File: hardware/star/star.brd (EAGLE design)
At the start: 139.4 x 187.9 mm, 170 parts, among them IC1 MAX481CSA, IC2 LD117AS12TR, IC22 LD117AS12TR, IC3 74HCT08D, IC4 7404D, IC8 MAX481CSA, K1 T90-12VDC-TL-A, K2 T90-12VDC-TL-A, K3 T90-12VDC-TL-A, K5 AQG22110, K6 AQG22110, Q1 35A/25V/8.5mΩ, Q2 35A/25V/8.5mΩ, Q3 35A/25V/8.5mΩ, Q4 35A/25V/8.5mΩ, T1 T_PNP_MMBT5401_CHANGJ_SOT23-B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, T2 T_PNP_MMBT5401_CHANGJ_SOT23-B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, T3 T_PNP_MMBT5401_CHANGJ_SOT23-B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, T4 T_PNP_MMBT5401_CHANGJ_SOT23-B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, U1 TCLT1600

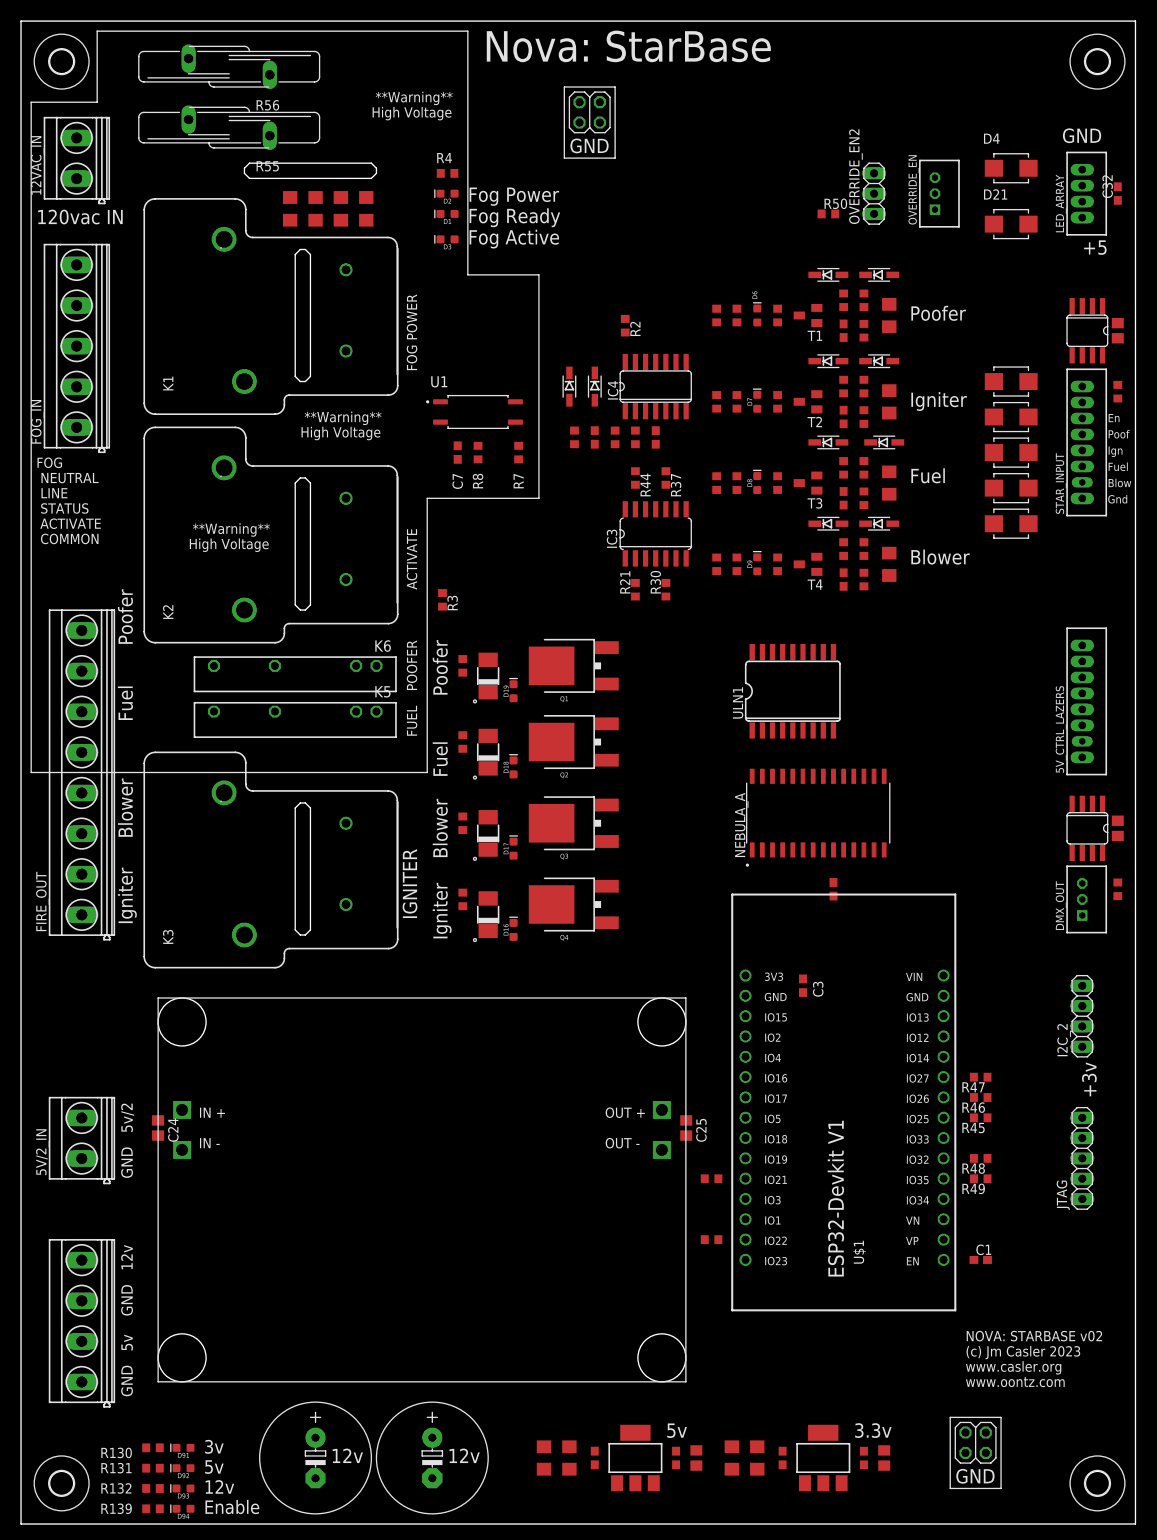
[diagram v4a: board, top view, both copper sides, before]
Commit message: Manual Routing Complete for v2
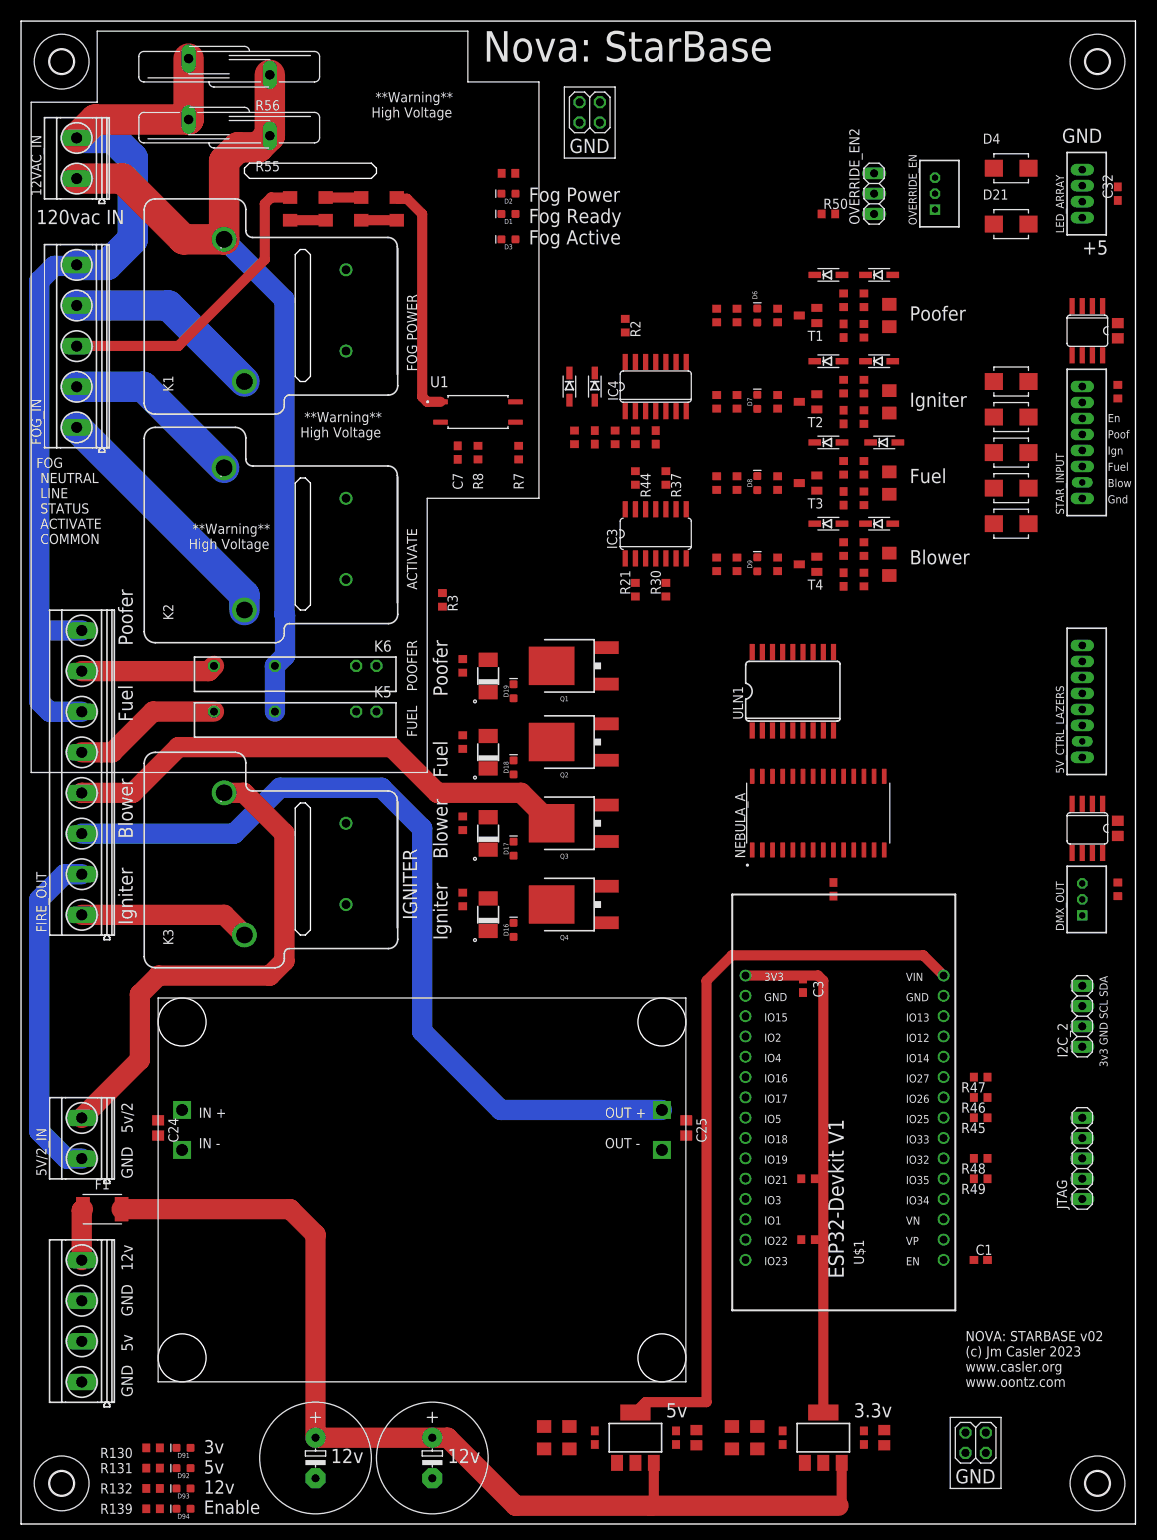
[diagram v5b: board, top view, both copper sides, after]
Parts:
- added F1: MF-MSMF-STYLE2_1, Fuse:FUSC4632X160
- moved R26 12.1 mm to (98.4, 35.6), turned to 0 degrees
- moved R27 12.1 mm to (98.4, 43.2), turned to 0 degrees
- moved D1 7.62 mm to (61.0, 163.8)
- moved D2 7.62 mm to (61.0, 166.4)
- moved D3 7.62 mm to (61.0, 160.7)
- moved R4 7.62 mm to (61.0, 168.9)
- moved R10 3.81 mm to (47.0, 164.5)
- moved C10 2.54 mm to (65.4, 10.8)
- moved C11 2.54 mm to (92.1, 10.8)
- moved C12 2.54 mm to (88.9, 10.8)
- moved C2 2.54 mm to (81.9, 10.8)
- moved C35 2.54 mm to (105.4, 10.8)
- moved C36 2.54 mm to (95.2, 10.8)
- moved C4 2.54 mm to (84.5, 10.8)
- moved C5 2.54 mm to (71.8, 10.8)
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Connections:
- new net N$59: F1.1, POWER_IN.4
- net +12V: now also C35.1, C6.1, F1.2, IC22.3; no longer POWER_IN.4
- net +5V: no longer C35.1, C6.1, IC22.3
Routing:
- net +12V: track 0.00 -> 130.9 mm
- net 120_NEUTRAL: track 0.00 -> 118.4 mm
- net 120_LINE: track 0.00 -> 108.8 mm
- net +14V: track 0.00 -> 106.5 mm
- net +5V: track 0.00 -> 94.2 mm
- net N$51: track 0.00 -> 65.1 mm
- net +3V3: track 0.00 -> 64.0 mm
- net +5V/2: track 0.00 -> 63.9 mm
- net GND3: track 0.00 -> 42.3 mm
- net N$7: track 0.00 -> 38.5 mm
- net N$15: track 0.00 -> 31.5 mm
- net N$11: track 0.00 -> 29.5 mm
- net N$14: track 0.00 -> 24.9 mm
- net N$13: track 0.00 -> 22.6 mm
- net N$53: track 0.00 -> 21.4 mm
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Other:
- board text added: "3v3 GND SCL SDA"
- board text removed: "+3v"

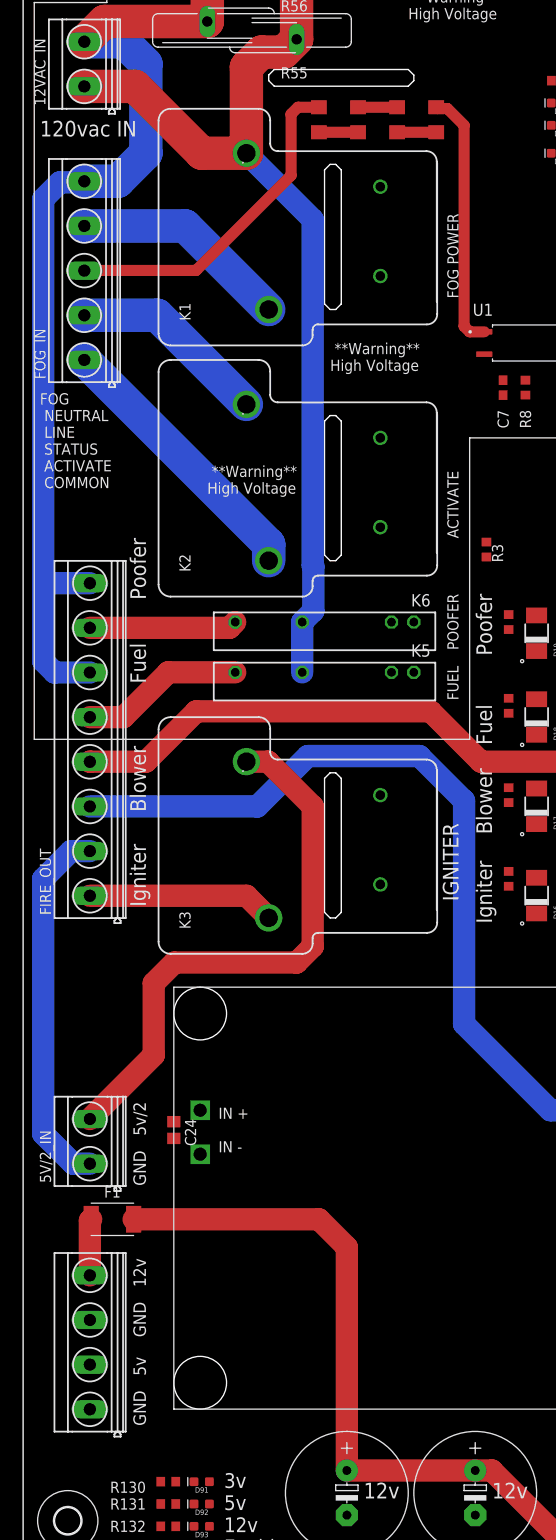
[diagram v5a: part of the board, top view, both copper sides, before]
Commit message: Swapped 1.5A fuse with 5A fuse
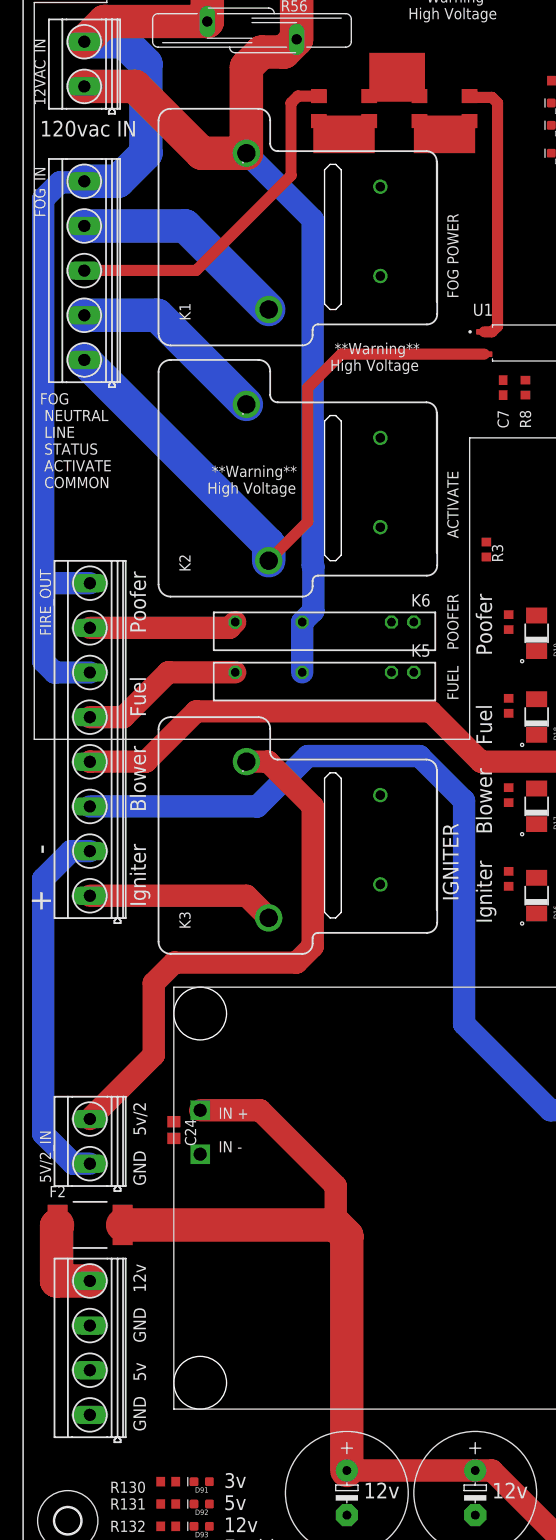
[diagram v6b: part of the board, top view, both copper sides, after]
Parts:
- removed F1: MF-MSMF-STYLE2_1, Fuse:FUSC4632X160
- added F2: 2920L200, 2920L200:SMD050F
- moved R10 4.02 mm to (50.8, 165.7)
- moved R11 2.84 mm to (45.1, 165.7)
- moved R12 1.80 mm to (39.4, 165.7)
- moved R13 1.27 mm to (33.7, 165.7)
- moved POWER_IN 0.63 mm to (7.62, 24.8)
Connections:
- net +12V: now also F2.2; no longer F1.2
- net N$59: now also F2.1; no longer F1.1
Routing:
- net N$15: track 31.5 -> 74.7 mm
- net +12V: track 130.9 -> 156.1 mm
- net N$59: track 6.43 -> 10.2 mm
- net N$7: track 38.5 -> 39.8 mm
- net N$9: track 4.45 -> 5.72 mm
- net N$8: track 4.45 -> 5.71 mm
- net N$10: track 4.45 -> 5.71 mm
- net N$11: track 29.5 -> 30.7 mm
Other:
- outline, holes or cut-outs redrawn
- board text added: "+ -"

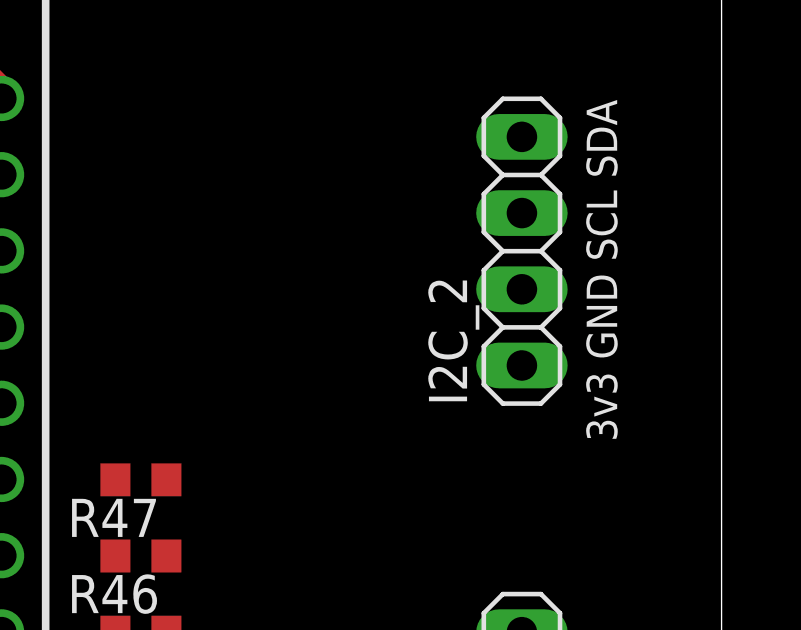
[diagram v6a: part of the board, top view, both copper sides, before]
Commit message: Updated labels
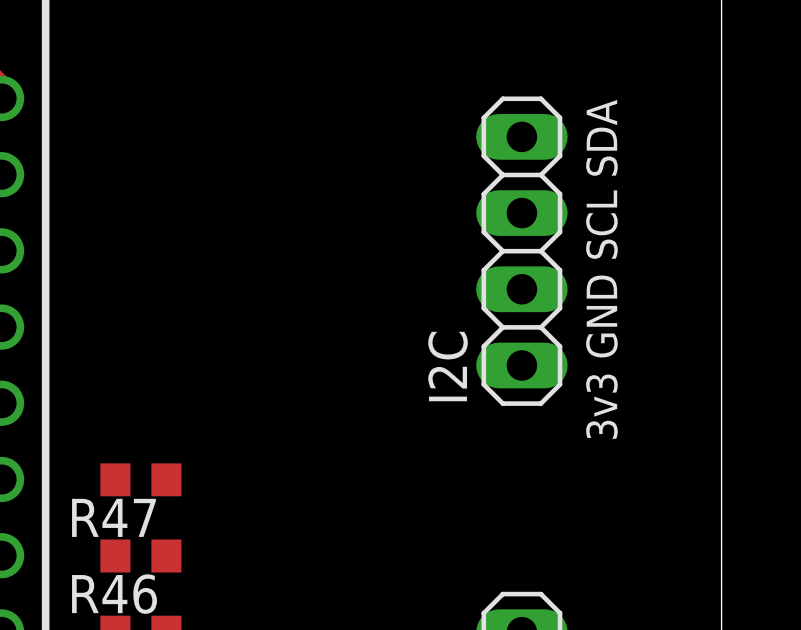
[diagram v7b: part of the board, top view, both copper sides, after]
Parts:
- renumbered I2C_2 to I2C
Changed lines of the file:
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@@
 <attribute name="VALUE" x="32.893" y="12.827" size="1.778" layer="27" ratio="10" rot="R270"/>
 </element>
-<element name="I2C_2" library="pinhead" library_urn="urn:adsk.eagle:library:325" package="1X04" package3d_urn="urn:adsk.eagle:package:22407/2" value="" x="132.715" y="63.5" smashed="yes" rot="R90">
+<element name="I2C" library="pinhead" library_urn="urn:adsk.eagle:library:325" package="1X04" package3d_urn="urn:adsk.eagle:package:22407/2" value="" x="132.715" y="63.5" smashed="yes" rot="R90">
 <attribute name="NAME" x="130.8862" y="58.3438" size="1.27" layer="25" ratio="10" rot="R90"/>
 <attribute name="POPULARITY" value="91" x="132.715" y="63.5" size="1.778" layer="27" rot="R90" display="off"/>
@@
 <contactref element="C36" pad="2"/>
 <contactref element="C89" pad="-"/>
-<contactref element="I2C_2" pad="2"/>
+<contactref element="I2C" pad="2"/>
 <contactref element="R7" pad="2"/>
 <contactref element="R8" pad="2"/>
@@
 <contactref element="C36" pad="1"/>
 <contactref element="IC22" pad="4"/>
-<contactref element="I2C_2" pad="1"/>
+<contactref element="I2C" pad="1"/>
 <contactref element="C14" pad="1"/>
 <contactref element="R2" pad="2"/>
@@
 <contactref element="U$1" pad="11"/>
 <contactref element="NEBULA_A" pad="13"/>
-<contactref element="I2C_2" pad="4"/>
+<contactref element="I2C" pad="4"/>
 <contactref element="R27" pad="1"/>
 <wire x1="106.68" y1="84.295" x2="132.715" y2="67.31" width="0" layer="19" extent="1-1"/>
@@
 <contactref element="U$1" pad="14"/>
 <contactref element="NEBULA_A" pad="12"/>
-<contactref element="I2C_2" pad="3"/>
+<contactref element="I2C" pad="3"/>
 <contactref element="R26" pad="1"/>
 <wire x1="105.41" y1="84.295" x2="132.715" y2="64.77" width="0" layer="19" extent="1-1"/>
@@
 <contactref element="D12" pad="A"/>
 <contactref element="Q1" pad="4"/>
+<contactref element="K6" pad="-"/>
 <contactref element="R60" pad="2"/>
-<contactref element="K6" pad="-"/>
 <wire x1="58.42" y1="108.07" x2="66.357" y2="107.315" width="0" layer="19" extent="1-1"/>
 <wire x1="55.245" y1="108.165" x2="58.42" y2="108.07" width="0" layer="19" extent="1-1"/>
@@
 <contactref element="D13" pad="A"/>
 <contactref element="Q2" pad="4"/>
+<contactref element="K5" pad="-"/>
 <contactref element="R61" pad="2"/>
-<contactref element="K5" pad="-"/>
 <wire x1="58.42" y1="98.545" x2="66.357" y2="97.79" width="0" layer="19" extent="1-1"/>
 <wire x1="55.245" y1="98.64" x2="58.42" y2="98.545" width="0" layer="19" extent="1-1"/>
@@
 <contactref element="D14" pad="A"/>
 <contactref element="FIRE_OUT" pad="4"/>
-<contactref element="R62" pad="2"/>
 <wire x1="7.595" y1="91.4189" x2="7.6161" y2="91.44" width="2.54" layer="1"/>
 <wire x1="13.97" y1="91.44" x2="19.685" y2="97.155" width="2.54" layer="1"/>
@@
 <wire x1="62.547" y1="91.44" x2="66.357" y2="87.63" width="2.54" layer="1"/>
 <wire x1="7.6161" y1="91.44" x2="13.97" y2="91.44" width="2.54" layer="1"/>
+<contactref element="R62" pad="2"/>
 <wire x1="55.245" y1="88.48" x2="58.42" y2="88.385" width="0" layer="19" extent="1-1"/>
 <wire x1="66.357" y1="87.63" x2="58.42" y2="88.385" width="0" layer="19" extent="1-1"/>
@@
 <contactref element="Q4" pad="4"/>
 <contactref element="D15" pad="A"/>
+<contactref element="K3" pad="2"/>
 <contactref element="R63" pad="2"/>
-<contactref element="K3" pad="2"/>
 <wire x1="58.42" y1="78.225" x2="66.357" y2="77.47" width="0" layer="19" extent="1-1"/>
 <wire x1="55.245" y1="78.955" x2="58.42" y2="78.225" width="0" layer="19" extent="1-1"/>
